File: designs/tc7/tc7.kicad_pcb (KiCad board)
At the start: 2 copper layers, 59.2 x 26.5 mm, 19 parts, among them J1001 SSM-104-L-SV, P1 TC2030, U1001 MCP6001-OT

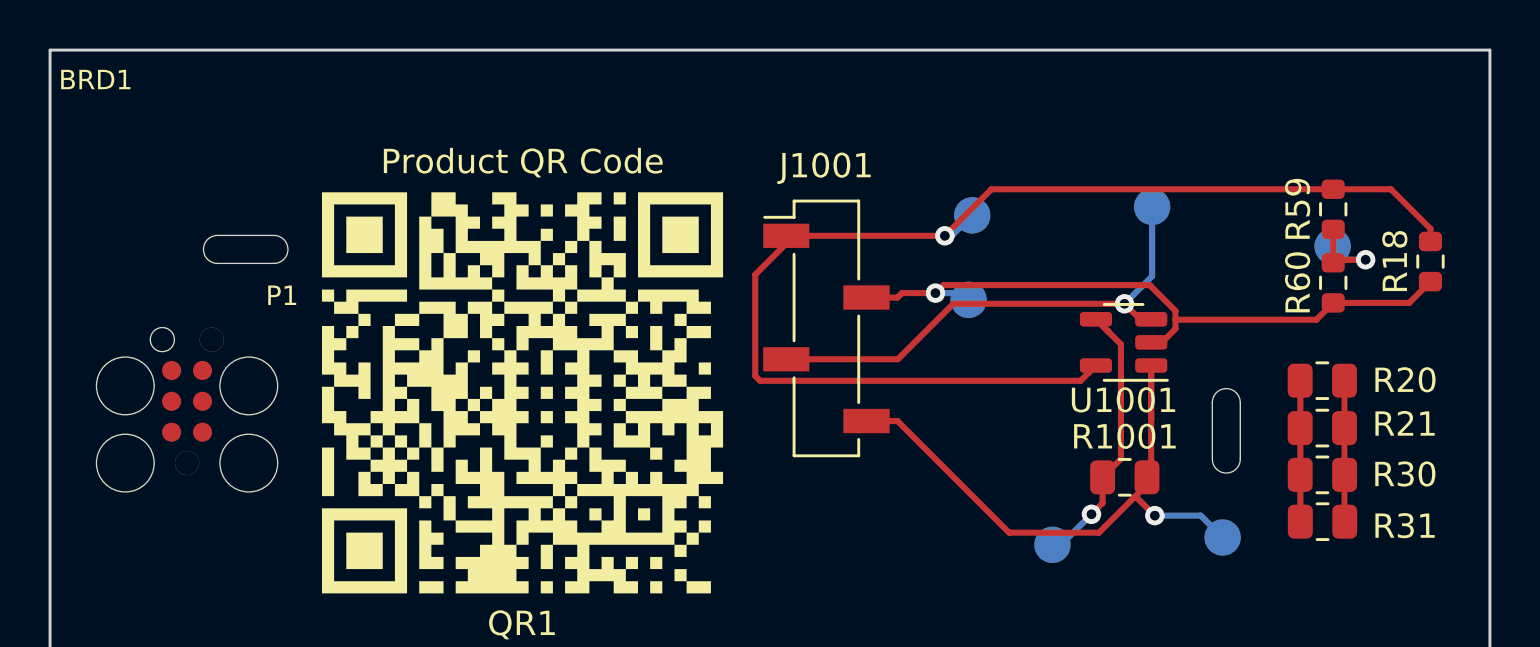
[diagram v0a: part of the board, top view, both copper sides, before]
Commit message: Tag KiCAD 6 version in tc7 directory for diffing
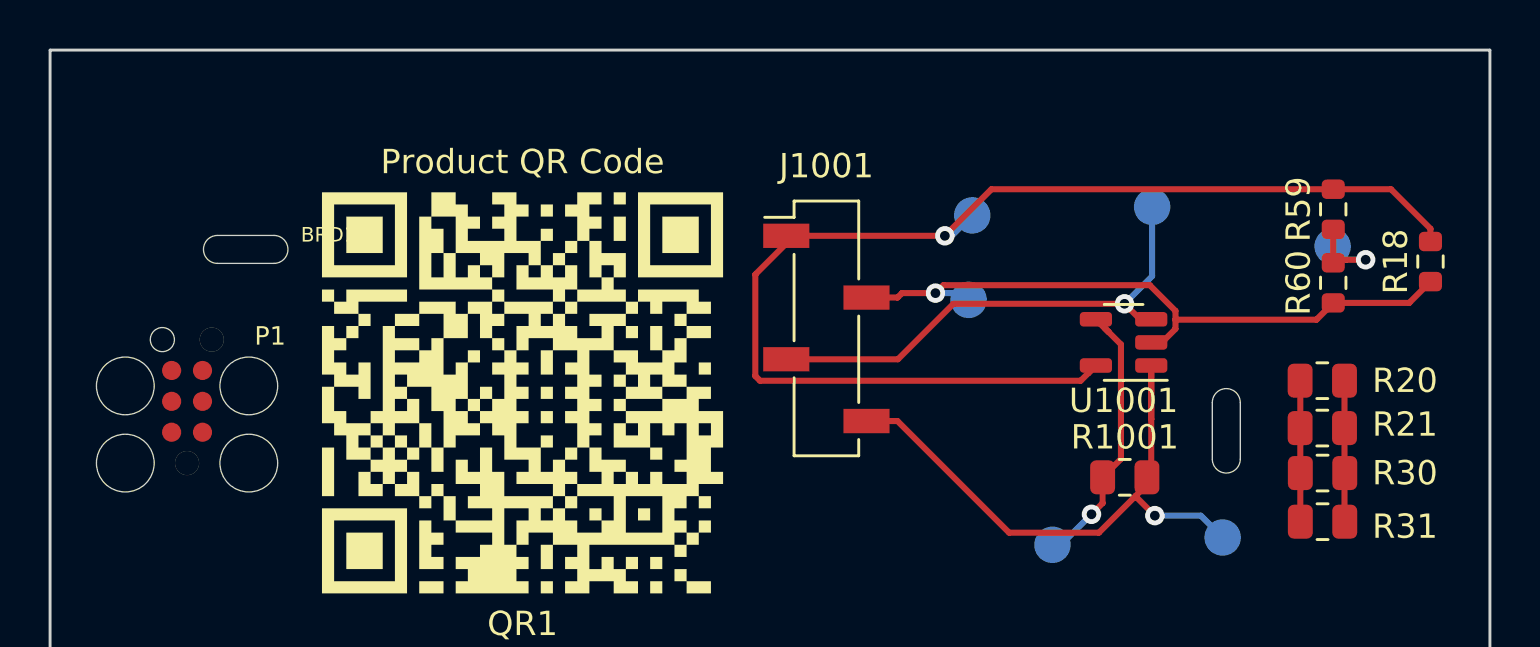
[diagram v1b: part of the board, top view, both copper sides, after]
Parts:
- moved R30 0.08 mm to (168.2, 101.2)
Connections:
- P1 pad 1: unconnected-(P1-Pin_1-Pad1) -> Net-(P1-Pad1)
- P1 pad 2: unconnected-(P1-Pin_2-Pad2) -> Net-(P1-Pad2)
- P1 pad 3: unconnected-(P1-Pin_3-Pad3) -> Net-(P1-Pad3)
- P1 pad 4: unconnected-(P1-Pin_4-Pad4) -> Net-(P1-Pad4)
- P1 pad 5: unconnected-(P1-Pin_5-Pad5) -> Net-(P1-Pad5)
- P1 pad 6: unconnected-(P1-Pin_6-Pad6) -> Net-(P1-Pad6)

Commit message: Back to kicad7
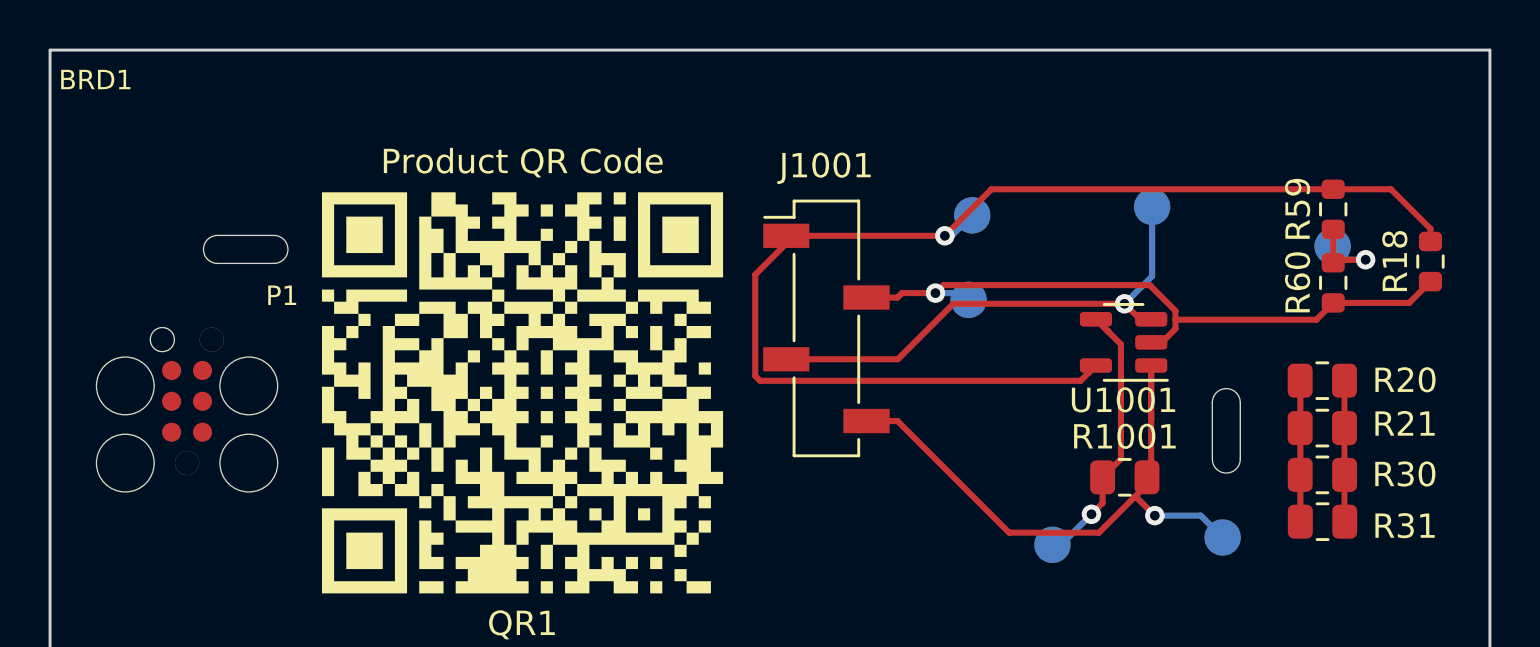
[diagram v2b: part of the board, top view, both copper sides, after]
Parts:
- moved R30 0.08 mm to (168.2, 101.3)
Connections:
- P1 pad 1: Net-(P1-Pad1) -> unconnected-(P1-Pin_1-Pad1)
- P1 pad 2: Net-(P1-Pad2) -> unconnected-(P1-Pin_2-Pad2)
- P1 pad 3: Net-(P1-Pad3) -> unconnected-(P1-Pin_3-Pad3)
- P1 pad 4: Net-(P1-Pad4) -> unconnected-(P1-Pin_4-Pad4)
- P1 pad 5: Net-(P1-Pad5) -> unconnected-(P1-Pin_5-Pad5)
- P1 pad 6: Net-(P1-Pad6) -> unconnected-(P1-Pin_6-Pad6)

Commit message: Demonstrate diff issue when PCB changes
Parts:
- BRD1: footprint tc7:DemoBoard -> tc7:biggerPCB
- moved BRD1 64.9 mm to (100.0, 150.0)
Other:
- board size 59.2 x 26.5 mm -> 70.6 x 123.5 mm
